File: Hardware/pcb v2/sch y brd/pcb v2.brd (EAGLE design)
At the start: 160 x 100 mm, 61 parts, among them J1 AVR_SPI_PRG_6PTH, J2 1981584-1, J3 HDMI, J4 HDMI, Q1 PMBT3904, Q2 PMBT3904, Q3 32.768kHz 12.5pF, U1 ATMEGA328P, U2 TXS0108EPWR-TSSOP20, U3 MB85RS16N, U4 ADP3338AKCZ-3.3RL7, U5 DS1307SO8, Y1 16Mhz

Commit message: Comienzo ruteo
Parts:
- moved JP1 579.2 mm to (60.0, 58.3)
- moved J2 574.8 mm to (54.2, 78.6), turned to 180 degrees
- moved JP2 550.3 mm to (92.4, 46.0)
- moved JP4 536.2 mm to (101.3, 18.9), turned to 90 degrees
- moved S1 521.6 mm to (7.29, 74.5)
- moved R10 498.4 mm to (50.4, 14.2)
- moved R1 497.7 mm to (45.3, 20.6)
- moved C11 486.5 mm to (16.1, 19.3)
- moved C10 481.0 mm to (23.7, 19.3)
- moved R15 475.5 mm to (30.0, 19.3)
- moved C15 466.3 mm to (70.7, 15.5)
- moved J3 446.4 mm to (81.0, 99.6), turned to 180 degrees
- moved U3 437.8 mm to (64.9, 28.5)
- moved C17 437.6 mm to (35.7, 25.9)
- moved J4 436.1 mm to (104.8, 99.6), turned to 180 degrees
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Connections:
- net N$23 renamed TX2_N
- net N$24 renamed TX1_P
- net N$25 renamed TX1_N
- net N$26 renamed TX0_P
- net N$27 renamed TX0_N
- net N$28 renamed CLK_P
- net N$29 renamed CLK_N
- net N$9 renamed TX2_P
- net +3V3: now also JP4.7; no longer JP4.2
- net +5V: now also JP4.9; no longer JP4.1
- net GND: now also JP4.2; no longer JP4.12
- net PD3: now also JP4.1; no longer JP4.7
- net PD4: now also JP4.12; no longer JP4.9
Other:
- board size 160 x 100 mm -> 120 x 80 mm

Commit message: empaquetados
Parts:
- removed C18: 10uF, rcl:E2,5-6
- removed G1: BATTERY-HOLDER_11.6MM, battery:CELL_RETAINER_11.6MM
- removed Q3: 32.768kHz 12.5pF, crystal:TC26H
- removed SG1: BUZZERPTH, SparkFun-Electromechanical:BUZZER-12MM
- removed Y1: 16Mhz, SparkFun-FreqCtrl:HC49US
- added CN1: (no value), adafruit:JST-PH-2-SMT
- added Q4: MC-306, crystal:MC-306
- added SP1: SPEAKER/PS12, adafruit:PS12
- added U6: (no value), seeedleo:BATTERY1225_SMT
- added Y2: CSTCE16M0V53-R0 16MHZ, SmartPrj:RESONATOR
- C15: value 10uF -> 1000uF; device rcl:E2,5-6 -> rcl:UD-10X10_NICHICON
- C16: value 1000uF -> (none); device rcl:E2,5-6 -> rcl:UD-5X5,8_NICHICON
- C5: value 22pF -> 1000uF; device rcl:C1206 -> rcl:UD-10X10_NICHICON
- C6: value 22pF -> 100uF; device rcl:C1206 -> rcl:C0805
- J3, J4: device partes v2:HDMI -> partes v2:0471511071
- R14: value 10k -> 4.7k
- moved C15 137.8 mm to (-62.8, 49.8)
- moved C16 135.9 mm to (-72.0, -22.0)
- moved U2 128.3 mm to (-47.2, -11.6)
- moved C6 111.9 mm to (-63.8, -24.2)
- moved U3 97.7 mm to (-23.4, -13.4)
- moved U4 96.2 mm to (-41.7, 18.5)
- moved C5 88.1 mm to (-58.5, 68.2)
- moved JP3 73.6 mm to (10.8, 32.9), turned to 90 degrees
- moved JP1 72.3 mm to (132.1, 63.5)
- moved R7 63.8 mm to (78.3, -10.2)
- moved U5 58.0 mm to (69.7, -16.8)
- moved J3 51.8 mm to (36.5, 73.1)
- moved J4 50.2 mm to (62.1, 73.1)
- moved C3 42.1 mm to (5.55, -6.92)
- moved MDL1 41.9 mm to (23.8, 26.4)
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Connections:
- removed net N$12: C6.1, U1.8, Y1.2
- new net N$9: U5.3, U6.2
- net +3V3: now also C16.+; no longer C18.+
- net +5V: now also C5.+, C6.1, SP1.P$1; no longer C16.+, SG1.+
- net GND: now also C5.-, JP2.6, U6.1, Y2.2; no longer C18.-, C5.2, G1.N-
- net N$11: now also Y2.1; no longer C5.1, Y1.1
- net N$2: now also Q4.4; no longer Q3.2
- net N$3: now also Q4.1; no longer Q3.1
- net N$4: now also U1.8, Y2.3; no longer G1.P+@1, G1.P+@2, U5.3
- net N$5: now also SP1.P$2; no longer SG1.-
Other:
- board size 120 x 80 mm -> 80 x 80 mm

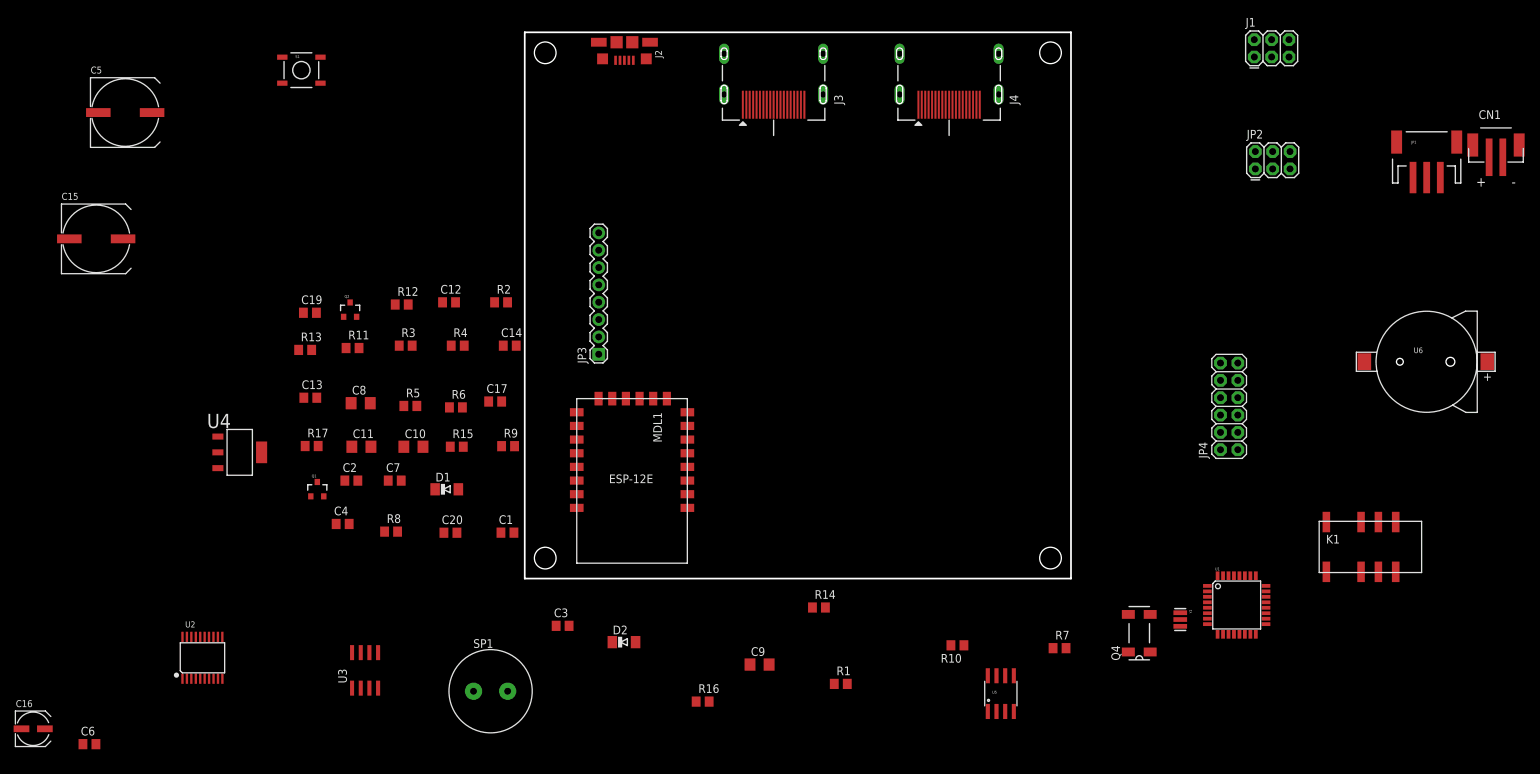
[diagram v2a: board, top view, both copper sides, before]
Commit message: posiciones componentes externos
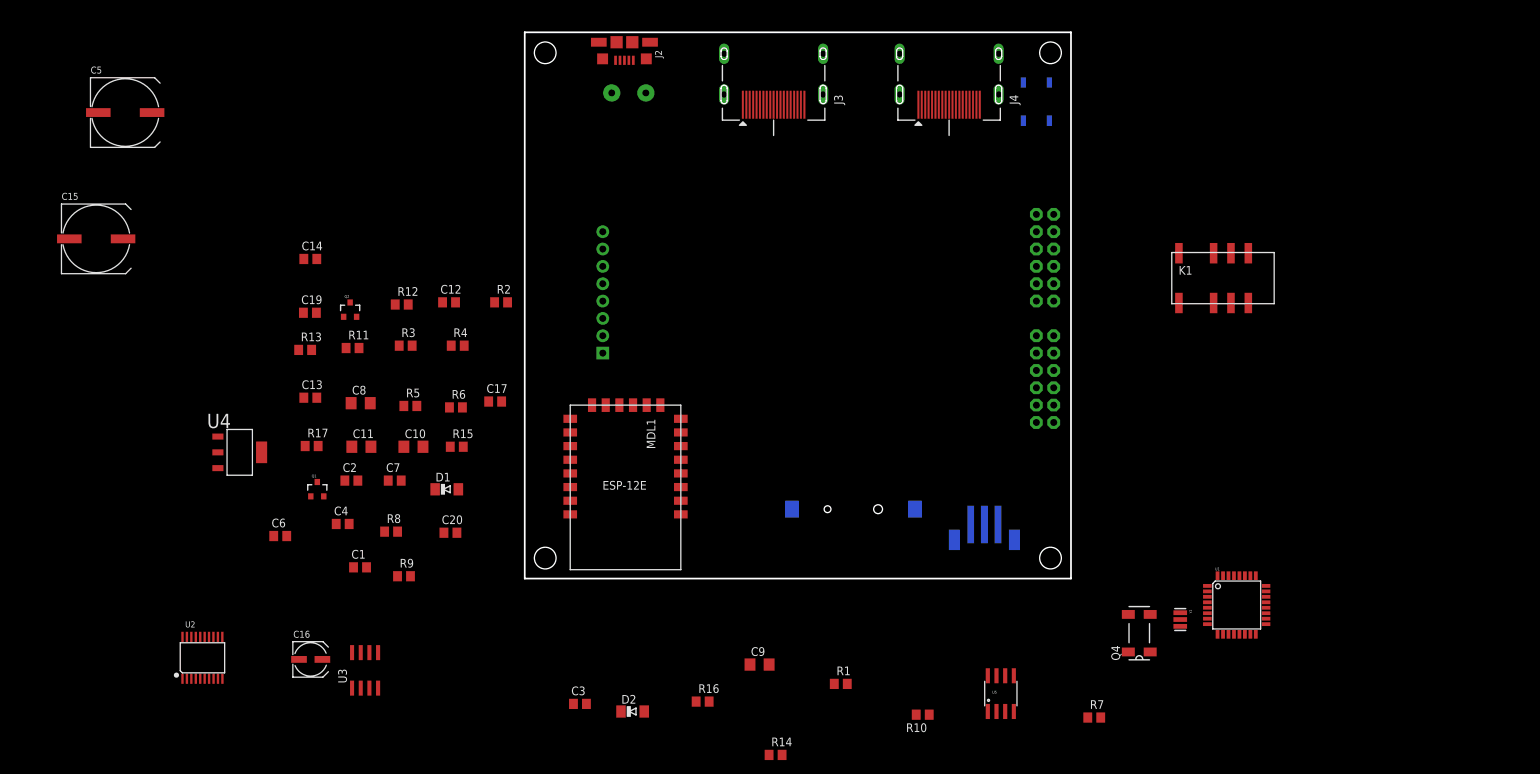
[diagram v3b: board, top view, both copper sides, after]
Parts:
- removed CN1: (no value), adafruit:JST-PH-2-SMT
- removed JP1: (no value), SparkFun-Connectors:JST-3-SMD
- removed JP3: (no value), SparkFun-Connectors:1X08
- added A1: RFID-RC522, partes v2:RFID-RC522
- added J5: JST-3, partes v2:B3B-PH-SM4-TB
- moved S1 107.7 mm to (74.9, 69.8), flipped to the bottom, turned to 90 degrees
- moved SP1 89.9 mm to (15.2, 71.1), flipped to the bottom
- moved U6 86.6 mm to (48.3, 10.2), flipped to the bottom, turned to 180 degrees
- moved K1 44.9 mm to (102.3, 44.0)
- moved J1 42.5 mm to (74.9, 48.3), flipped to the bottom, turned to 90 degrees
- moved C16 41.9 mm to (-31.4, -11.8)
- moved C6 41.3 mm to (-35.8, 6.23)
- moved JP2 37.5 mm to (74.9, 40.6), flipped to the bottom, turned to 90 degrees
- moved C14 31.9 mm to (-31.4, 46.8)
- moved JP4 29.8 mm to (74.9, 22.9), flipped to the bottom
- moved R9 24.4 mm to (-17.7, 0.34)
- moved R14 22.5 mm to (36.7, -25.8)
- moved C1 22.2 mm to (-24.1, 1.65)
- moved C3 11.7 mm to (8.09, -18.4)
- moved R10 11.4 mm to (58.3, -19.9)
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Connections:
- net +3V3: now also A1.3.3V; no longer JP3.8
- net +5V: now also J5.3; no longer JP1.3
- net GND: now also A1.GND, J5.1; no longer JP1.1, JP3.6
- net LED: now also J5.2; no longer JP1.2
- net RFID_MISO_3V3: now also A1.MISO; no longer JP3.4
- net RFID_MOSI_3V3: now also A1.MOSI; no longer JP3.3
- net RFID_OC_NRST: now also A1.RST; no longer JP3.7
- net RFID_SCK_3V3: now also A1.SCK; no longer JP3.2
- net RFID_SS_3V3: now also A1.SDA; no longer JP3.1
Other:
- board text added: "Gravedad caja horizontal"
- board text added: "Gravedad caja vertical"

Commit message: ruteo tdms
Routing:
- net N$30: track 0.00 -> 71.0 mm
- net CLK_N: track 0.00 -> 49.5 mm
- net CLK_P: track 0.00 -> 49.5 mm
- net TX2_N: track 0.00 -> 49.2 mm
- net TX2_P: track 0.00 -> 49.2 mm
- net TX1_P: track 0.00 -> 49.1 mm
- net TX1_N: track 0.00 -> 49.1 mm
- net TX0_P: track 0.00 -> 48.9 mm
- net TX0_N: track 0.00 -> 48.7 mm
- added copper zone on layer 1, net GND

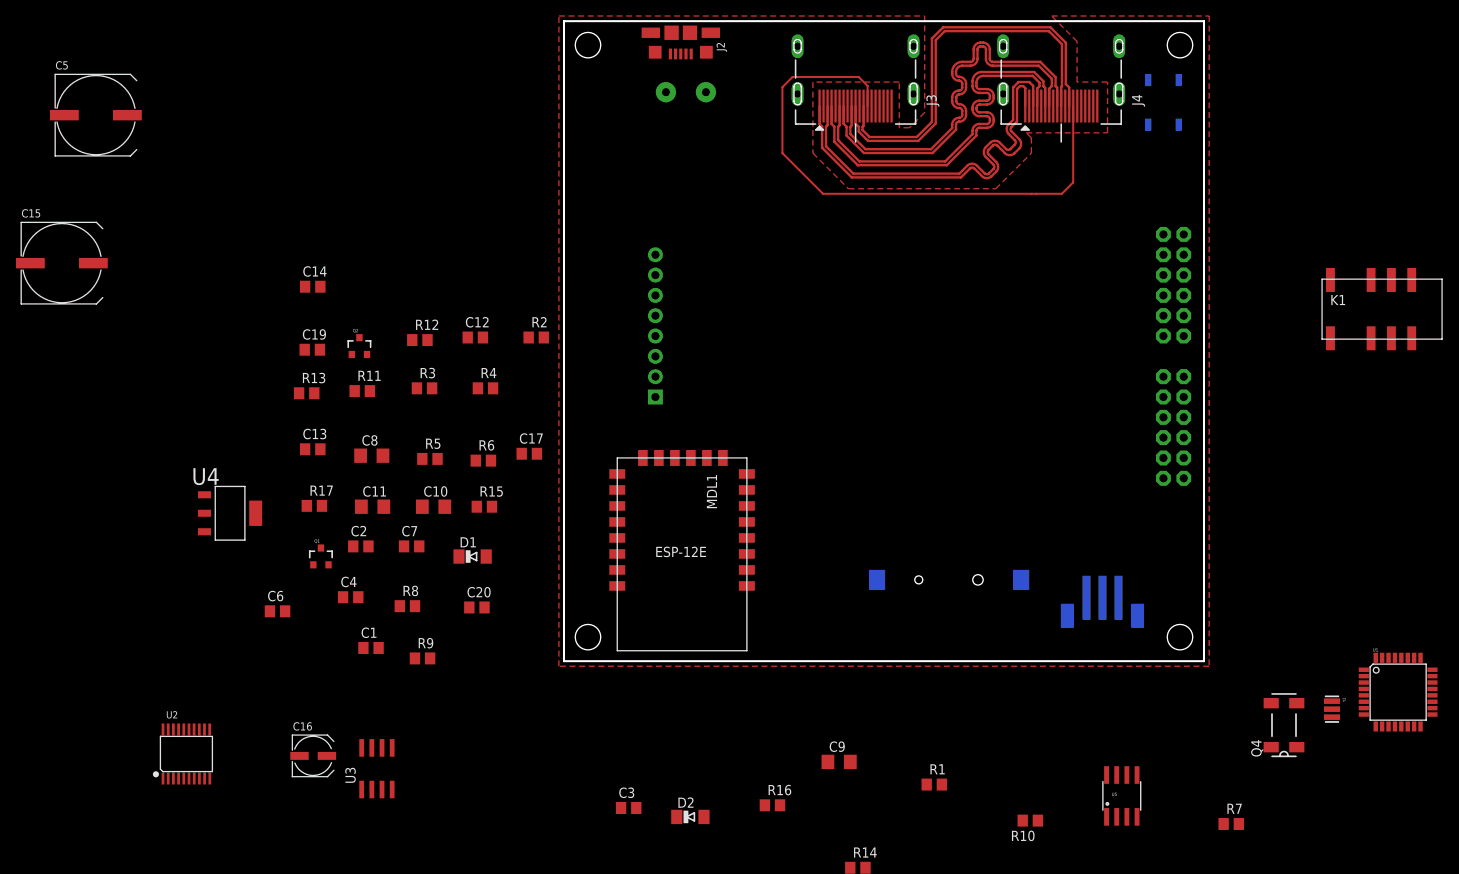
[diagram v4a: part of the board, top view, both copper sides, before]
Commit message: ruteo hdmi completo
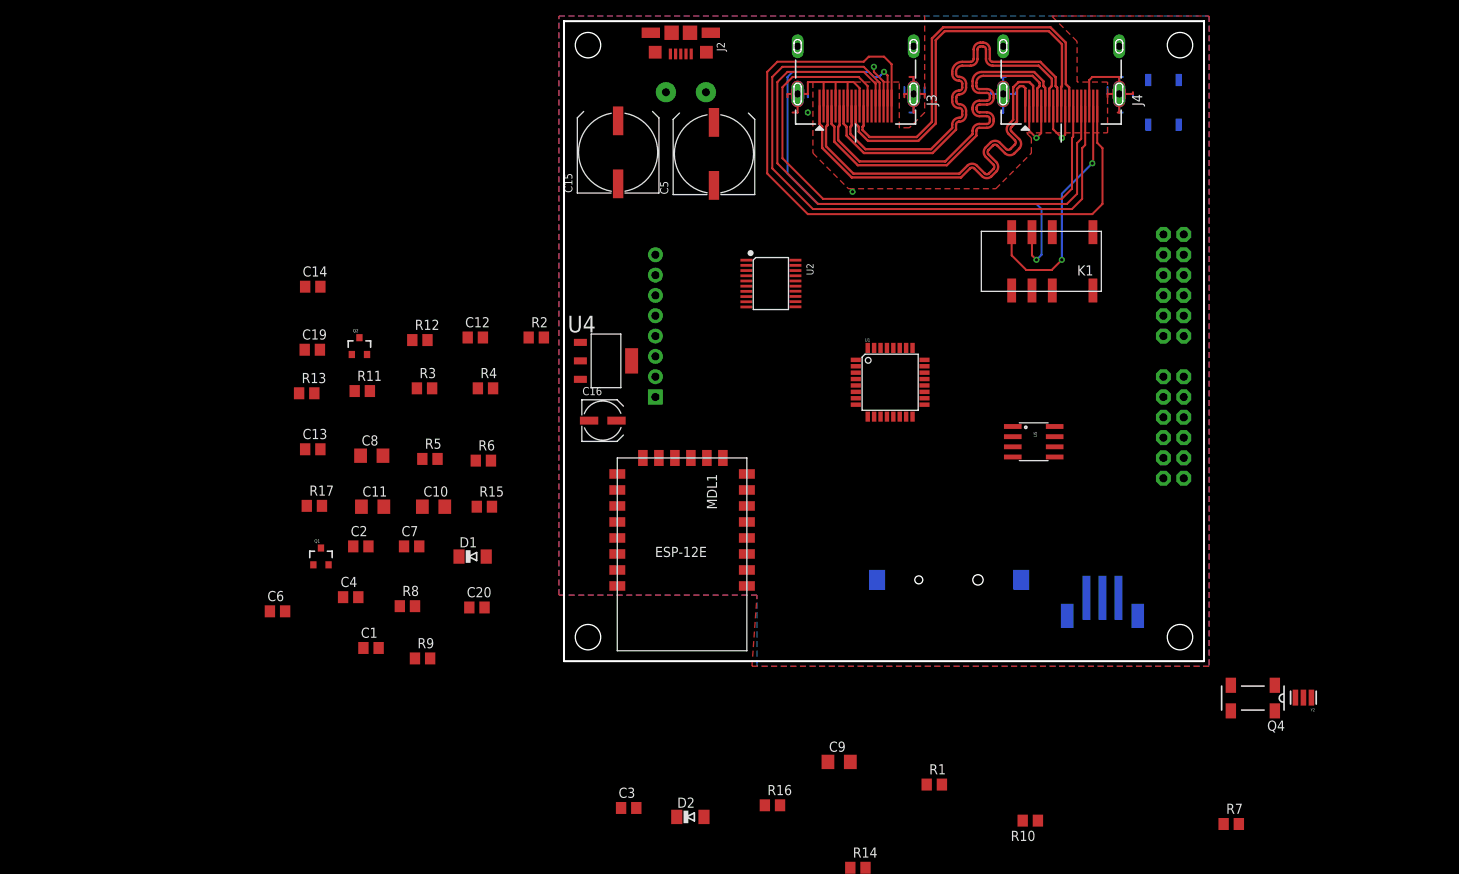
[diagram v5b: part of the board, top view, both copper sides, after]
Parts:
- removed C17: 100nF, rcl:C0805
- removed U3: MB85RS16N, partes v2:SOP8
- moved U2 93.8 mm to (25.9, 47.2), turned to 270 degrees
- moved C5 77.4 mm to (18.7, 63.4), turned to 90 degrees
- moved U1 74.4 mm to (40.8, 34.9)
- moved C15 70.9 mm to (6.76, 63.6), turned to 90 degrees
- moved C16 55.4 mm to (4.83, 30.1)
- moved U4 50.7 mm to (5.25, 37.5)
- moved U5 45.6 mm to (58.7, 27.4), turned to 270 degrees
- moved K1 43.0 mm to (59.7, 50.0), turned to 180 degrees
- moved Q4 5.16 mm to (86.1, -4.62), turned to 180 degrees
- moved Y2 3.85 mm to (92.4, -4.56), turned to 180 degrees
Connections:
- removed net N$39: U2.8, U3.1
- new net ESP_GPIO13_3V3: MDL1.7, U2.8
- net +3V3: no longer C17.1, U3.3, U3.7, U3.8
- net GND: no longer C17.2, U3.4
- net RFID_MISO_3V3: no longer U3.2
- net RFID_MOSI_3V3: no longer U3.5
- net RFID_SCK_3V3: no longer U3.6
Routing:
- net GND: track 0.00 -> 101.5 mm, vias 0 -> 5
- net N$33: track 0.00 -> 91.7 mm
- net N$32: track 0.00 -> 82.2 mm
- net N$31: track 0.00 -> 77.6 mm
- net HDMI_A_5V: track 0.00 -> 73.3 mm, vias 0 -> 2
- net HDMI_B_5V: track 0.00 -> 31.3 mm, vias 0 -> 2
- net N$30: track 71.0 -> 72.3 mm
- added copper zone on layer 16, net GND

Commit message: avance ruteo
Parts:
- removed C19: 1uF, rcl:C0805
- removed C20: 100nF, rcl:C0805
- removed JP4: 2X6 FEMALE, SparkFun-Connectors:2X6
- removed Q4: MC-306, crystal:MC-306
- removed U5: DS1307SO8, SparkFun-FreqCtrl:SO08
- removed U6: (no value), seeedleo:BATTERY1225_SMT
- removed Y2: CSTCE16M0V53-R0 16MHZ, SmartPrj:RESONATOR
- added BT1: 1225BAT, partes v2:BHSD-1225-SM
- added C17: 1uF, rcl:C0805
- added C18: 100nF, rcl:C0603
- added JP1: FEMALE 2x3, SparkFun-Connectors:2X3
- added Q3: MC-306, crystal:MC-306
- added U3: ADP3338AKCZ-3.3RL7, ADI-Phase-2:SOT230P700X180-4N
- added Y1: CSTCE16M0V53-R0 16MHZ, SmartPrj:RESONATOR
- C1, C12, C2, C3, C4: device rcl:C0805 -> rcl:C0603
- C10: value 10uF -> 100nF; device rcl:C1206 -> rcl:C0603
- C11: value 1uF -> 100nF; device rcl:C1206 -> rcl:C0603
- C13, C7: value 100nF -> 100uF; device rcl:C0805 -> rcl:C1206
- C14: value 100nF -> 1200uF; device rcl:C0805 -> rcl:UD-10X10_NICHICON
- C15: value 1000uF -> 1200uF
- C16: value (none) -> 10uF
- C5: value 1000uF -> 100nF; device rcl:UD-10X10_NICHICON -> rcl:C0603
- C6: value 100uF -> 470pF; device rcl:C0805 -> rcl:C0603
- C8: value 470pF -> 10uF; device rcl:C1206 -> rcl:C0805
- C9: value 100uF -> 1uF; device rcl:C1206 -> rcl:C0805
- J4: value HDMI -> JST-3; device partes v2:0471511071 -> partes v2:B3B-PH-SM4-TB
- J5: value JST-3 -> HDMI; device partes v2:B3B-PH-SM4-TB -> partes v2:0471511071
- JP2: value FEMALE 2x3 -> 2X6 FEMALE; device SparkFun-Connectors:2X3 -> SparkFun-Connectors:2X6
- R11, R16, R17, R2, R3, R4, R5, R6, R7, R8: device rcl:R0805 -> rcl:R0603
- R14: value 4.7k -> 10k; device rcl:R0805 -> rcl:R0603
- U4: value ADP3338AKCZ-3.3RL7 -> DS1307SO8; device ADI-Phase-2:SOT230P700X180-4N -> SparkFun-FreqCtrl:SO08
- moved R17 107.6 mm to (76.2, 13.3), flipped to the bottom, turned to 180 degrees
- moved Q1 96.9 mm to (60.3, 47.0), flipped to the bottom, turned to 270 degrees
- moved R15 95.4 mm to (74.9, 62.9), flipped to the bottom
- moved R9 86.9 mm to (55.2, 47.6), flipped to the bottom, turned to 180 degrees
- moved D2 84.9 mm to (63.5, 50.8), flipped to the bottom, turned to 270 degrees
- moved R8 82.6 mm to (49.5, 52.1), turned to 180 degrees
- moved R7 77.1 mm to (49.5, 48.9), flipped to the bottom
- moved C13 71.4 mm to (21.6, 74.3), turned to 90 degrees
- moved C1 69.7 mm to (38.7, 31.8)
- moved U4 69.1 mm to (69.2, 11.4), turned to 270 degrees
- moved C4 66.6 mm to (36.8, 27.9), turned to 180 degrees
- moved J4 65.7 mm to (67.3, 7.62), flipped to the bottom
- moved J5 65.7 mm to (62.1, 73.1), flipped to the top
- moved C2 63.2 mm to (36.8, 25.4), turned to 180 degrees
- moved R10 61.3 mm to (36.8, 37.5), turned to 0 degrees
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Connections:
- net +3V3: now also C7.1, C8.1, JP2.7, U3.2, U3.4; no longer C11.1, C14.1, JP4.7, U4.2, U4.4
- net +5V: now also C11.1, C14.+, C17.1, C18.1, J4.3, JP2.9, U3.3, U4.8; no longer C19.1, C20.1, C5.+, C6.1, J5.3, JP4.9, U4.3, U5.8
- net ADC6: now also JP2.3; no longer JP4.3
- net ADC7: now also JP2.5; no longer JP4.5
- net CLK_N: now also J5.P$12; no longer J4.P$12
- net CLK_P: now also J5.P$10; no longer J4.P$10
- net ESP_OC_NPROG: now also JP1.5; no longer JP2.5
- net ESP_OC_NRST: now also C6.1, JP1.4; no longer C8.1, JP2.4
- net ESP_RX_3V3: now also JP1.1; no longer JP2.1
- net ESP_TX_3V3: now also JP1.2; no longer JP2.2
- net GND: now also BT1.V-, C14.-, C17.2, C18.2, C5.2, J4.1, J5.P$11, J5.P$17, J5.P$2, J5.P$20, J5.P$21, J5.P$22, J5.P$23, J5.P$5, J5.P$8, JP1.6, JP2.11, JP2.2, U3.1, U4.4, Y1.2; no longer C14.2, C19.2, C20.2, C5.-, J4.P$11, J4.P$17, J4.P$2, J4.P$20, J4.P$21, J4.P$22, J4.P$23, J4.P$5, J4.P$8, J5.1, JP2.6, JP4.11, JP4.2, U4.1, U5.4, U6.1, Y2.2
- net HDMI_B_5V: now also J5.P$18; no longer J4.P$18
- net LED: now also J4.2; no longer J5.2
- net LVLSHF_OC_OE: now also JP1.3; no longer JP2.3
- net N$11: now also Y1.1; no longer Y2.1
- net N$2: now also Q3.4, U4.1; no longer Q4.4, U5.1
- net N$3: now also Q3.1, U4.2; no longer Q4.1, U5.2
- net N$30: now also J5.P$13; no longer J4.P$13
- net N$31: now also J5.P$15; no longer J4.P$15
- net N$32: now also J5.P$16; no longer J4.P$16
- net N$33: now also J5.P$19; no longer J4.P$19
- net N$4: now also Y1.3; no longer Y2.3
- net N$6: now also U4.7; no longer U5.7
- net N$9: now also BT1.V+, U4.3; no longer U5.3, U6.2
- net PB2: now also JP2.6; no longer JP4.6
- net PD3: now also JP2.1; no longer JP4.1
- net PD4: now also JP2.12; no longer JP4.12
- net PD5: now also JP2.4; no longer JP4.4
- net RST_ATM: now also C5.1; no longer C7.1
- net SCL: now also JP2.10, U4.6; no longer JP4.10, U5.6
- net SDA: now also JP2.8, U4.5; no longer JP4.8, U5.5
- net TX0_N: now also J5.P$9; no longer J4.P$9
- net TX0_P: now also J5.P$7; no longer J4.P$7
- net TX1_N: now also J5.P$6; no longer J4.P$6
- net TX1_P: now also J5.P$4; no longer J4.P$4
- net TX2_N: now also J5.P$3; no longer J4.P$3
- net TX2_P: now also J5.P$1; no longer J4.P$1
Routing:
- net +5V: track 0.00 -> 89.0 mm, vias 0 -> 2
- net +3V3: track 0.00 -> 76.4 mm, vias 0 -> 34
- net BOTON: track 0.00 -> 35.3 mm
- net ESP_OC_NPROG: track 0.00 -> 28.6 mm, vias 0 -> 3
- net SCL: track 0.00 -> 24.7 mm
- net ESP_TX_3V3: track 0.00 -> 24.5 mm
- net BUZZER: track 0.00 -> 24.3 mm, vias 0 -> 1
- net SDA: track 0.00 -> 22.5 mm, vias 0 -> 1
- net ESP_RX_3V3: track 0.00 -> 21.7 mm
- net RST_ATM_3V3: track 0.00 -> 16.5 mm
- net HDMI_A_5V: track 73.3 -> 86.6 mm, vias 2 -> 4
- net N$15: track 0.00 -> 13.2 mm, vias 0 -> 1
- net LED: track 0.00 -> 12.9 mm
- net N$13: track 0.00 -> 9.52 mm, vias 0 -> 1
- net N$9: track 0.00 -> 8.19 mm, vias 0 -> 1
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- added copper zone on layer 1, net +3V3
- added copper zone on layer 16, net +3V3
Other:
- board text added: "SET POLYGON_RATSNEST ON / OFF; Ancho pista min: 10mil Via drill: 15mil Via diam: 31mil"
